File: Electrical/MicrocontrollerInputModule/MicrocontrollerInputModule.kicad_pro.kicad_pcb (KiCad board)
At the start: 2 copper layers, 33.8 x 131 mm, 47 parts, among them J1 Conn_02x04_Odd_Even, J2 Conn_01x16, J3 Conn_01x10, SW1 KXT3, SW2 KXT3, U1 W25Q16JVUXIQ, U2 RP2040, Y1 12.000MHz

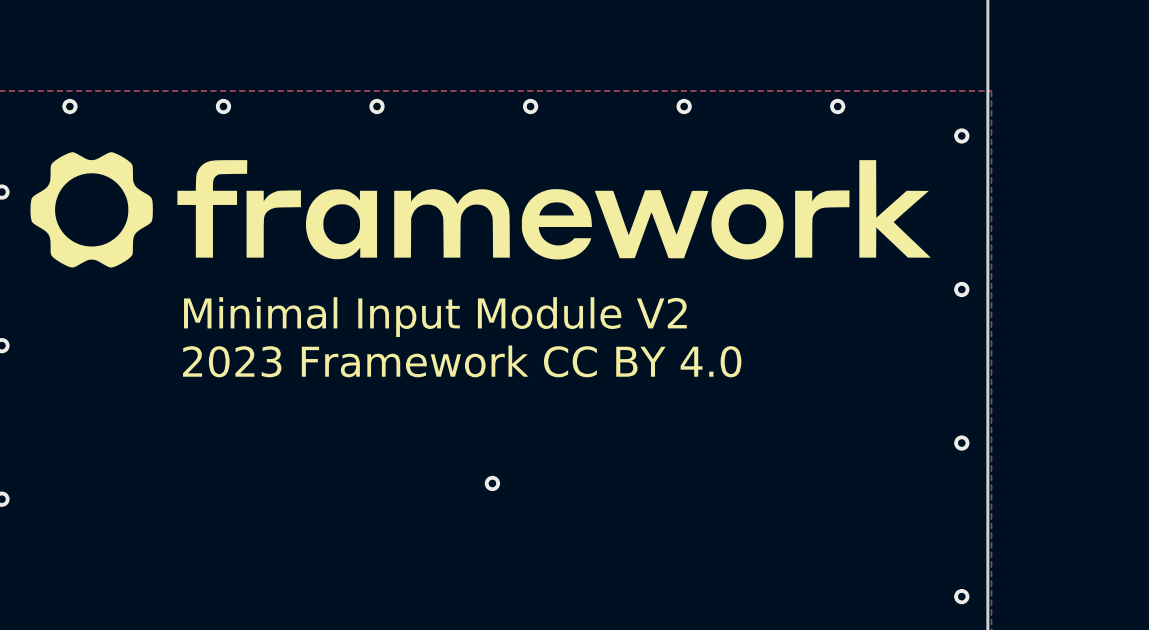
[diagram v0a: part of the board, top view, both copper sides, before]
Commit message: Rename to Microcontroller Input Module
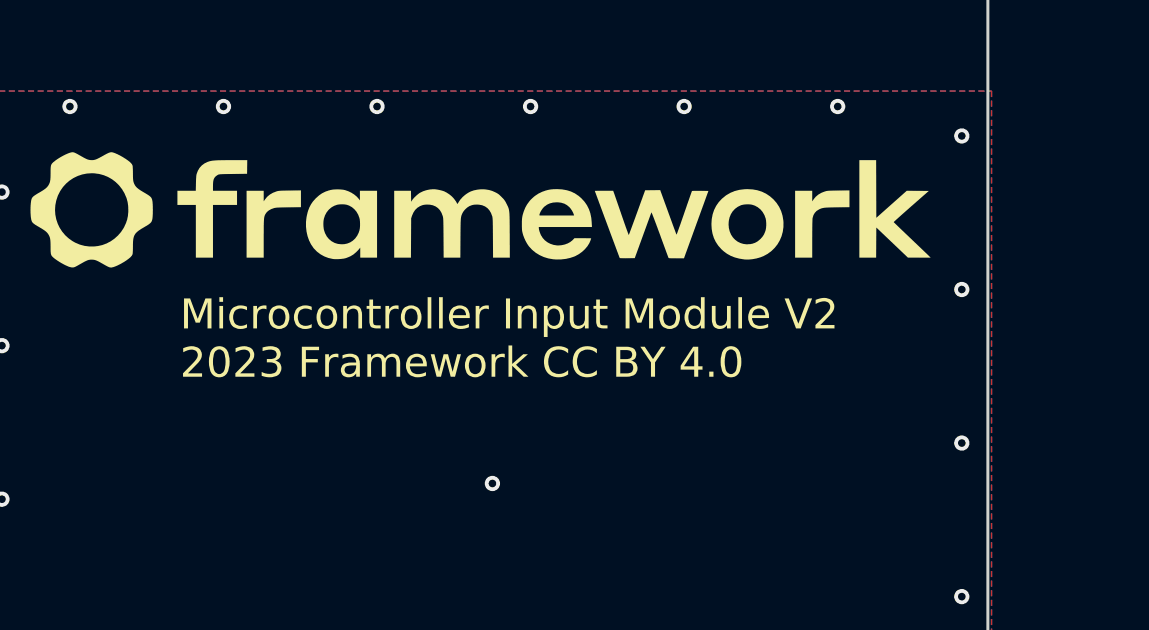
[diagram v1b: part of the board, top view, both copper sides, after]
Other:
- board text added: "Microcontroller Input Module V2 2023 Framework CC BY 4.0"
- board text removed: "Minimal Input Module V2 2023 Framework CC BY 4.0"
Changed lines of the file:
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@@
   )
   (paper "A4")
+  (title_block
+    (title "Microcontroller Input Module")
+    (date "2023-03-12")
+    (rev "V2")
+    (company "Framework Computer Inc")
+    (comment 1 "https://frame.work")
+    (comment 2 "https://github.com/FrameworkComputer/InputModules")
+    (comment 3 "This work is licensed under a Creative Commons Attribution 4.0 International License")
+  )
   (layers
     (0 "F.Cu" signal)
@@
     (effects (font (size 1 1) (thickness 0.15)) (justify right))
   )
-  (gr_text "Minimal Input Module V2\n2023 Framework CC BY 4.0" (at 56.896 66.294) (layer "F.SilkS")
+  (gr_text "Microcontroller Input Module V2\n2023 Framework CC BY 4.0" (at 56.896 66.294) (layer "F.SilkS")
     (effects (font (size 1 1) (thickness 0.15)) (justify left))
   )
